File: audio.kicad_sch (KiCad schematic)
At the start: 27 parts, among them U13 PCM5102APWR, U14 PAM8908JER

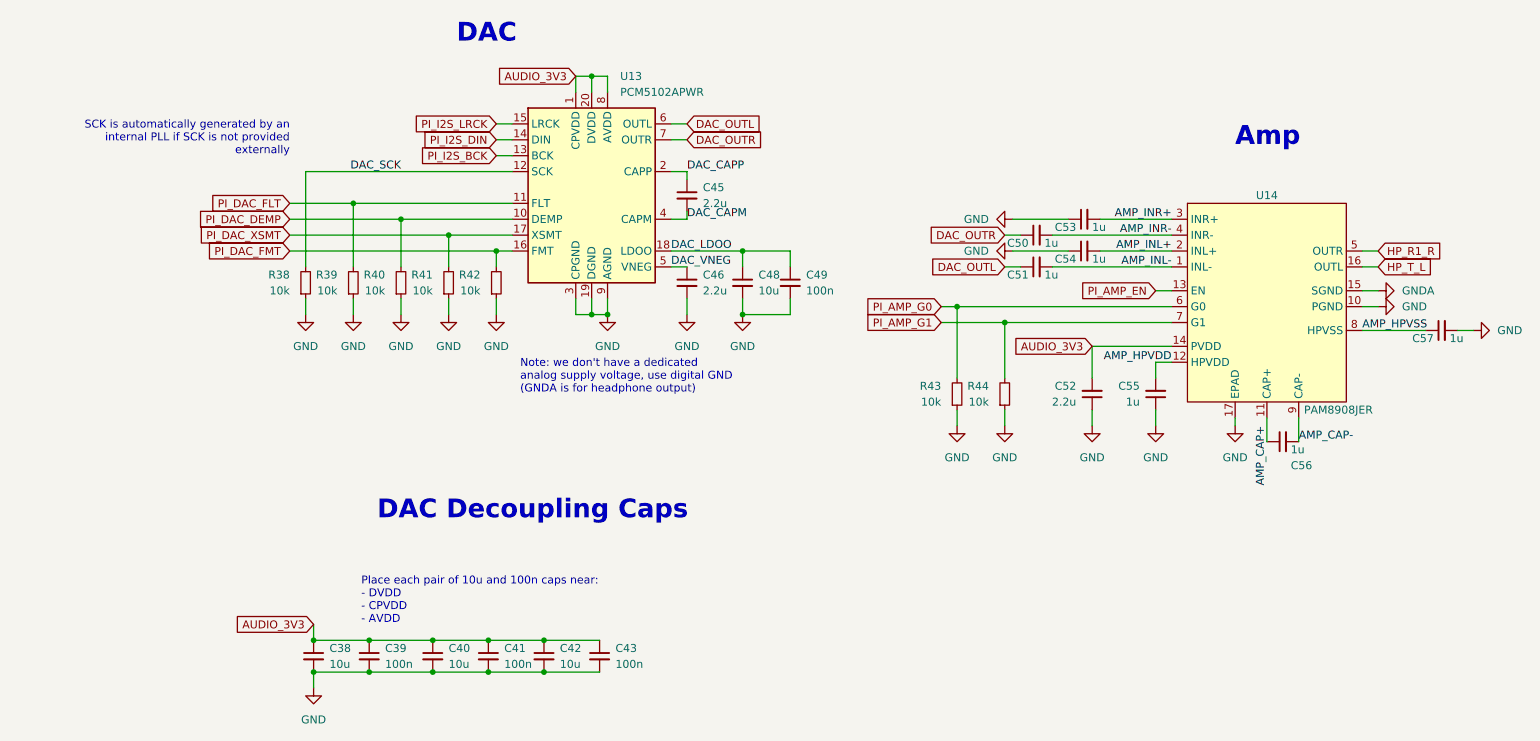
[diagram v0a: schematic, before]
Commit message: ci: test marking parts in sch for bom
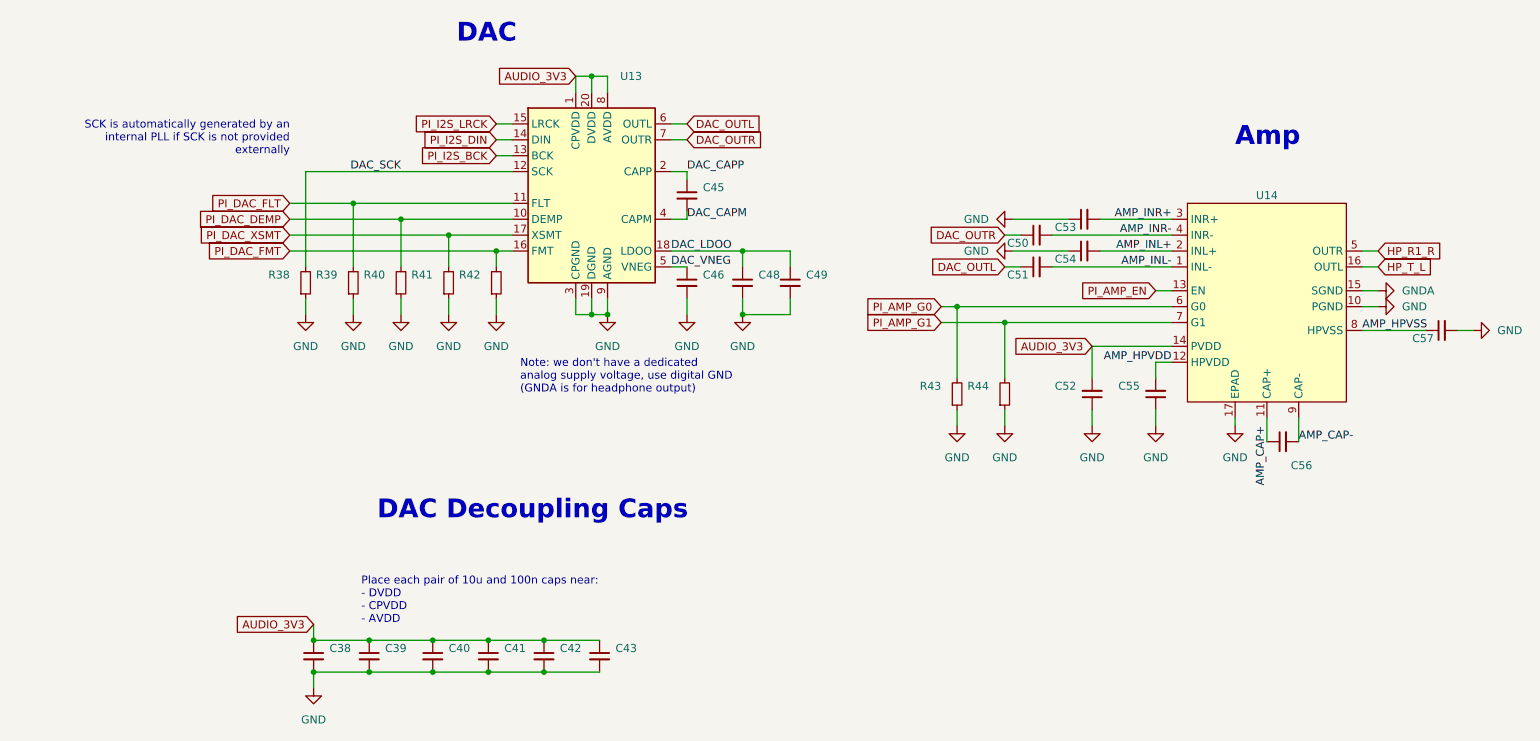
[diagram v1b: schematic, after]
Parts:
- C38, C40, C42, C48: value 10u -> (none); footprint Capacitor_SMD:C_0402_1005Metric -> (none)
- C39, C41, C43, C49: value 100n -> (none); footprint Capacitor_SMD:C_0402_1005Metric -> (none)
- C45, C46, C52: value 2.2u -> (none); footprint Capacitor_SMD:C_0402_1005Metric -> (none)
- C50, C51, C53, C54, C55, C56, C57: value 1u -> (none); footprint Capacitor_SMD:C_0402_1005Metric -> (none)
- R38, R39, R40, R41, R42, R43, R44: value 10k -> (none); footprint Resistor_SMD:R_0402_1005Metric -> (none)
- U13: value PCM5102APWR -> (none); footprint Package_SO:TSSOP-20_4.4x6.5mm_P0.65mm -> (none)
- U14: value PAM8908JER -> (none); footprint Gigahawk:QFN-16-1EP_3x3mm_P0.5mm_EP1.7x1.7mm -> (none)
